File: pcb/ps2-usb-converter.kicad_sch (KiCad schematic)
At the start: 22 parts, among them J1 Mini-DIN-6

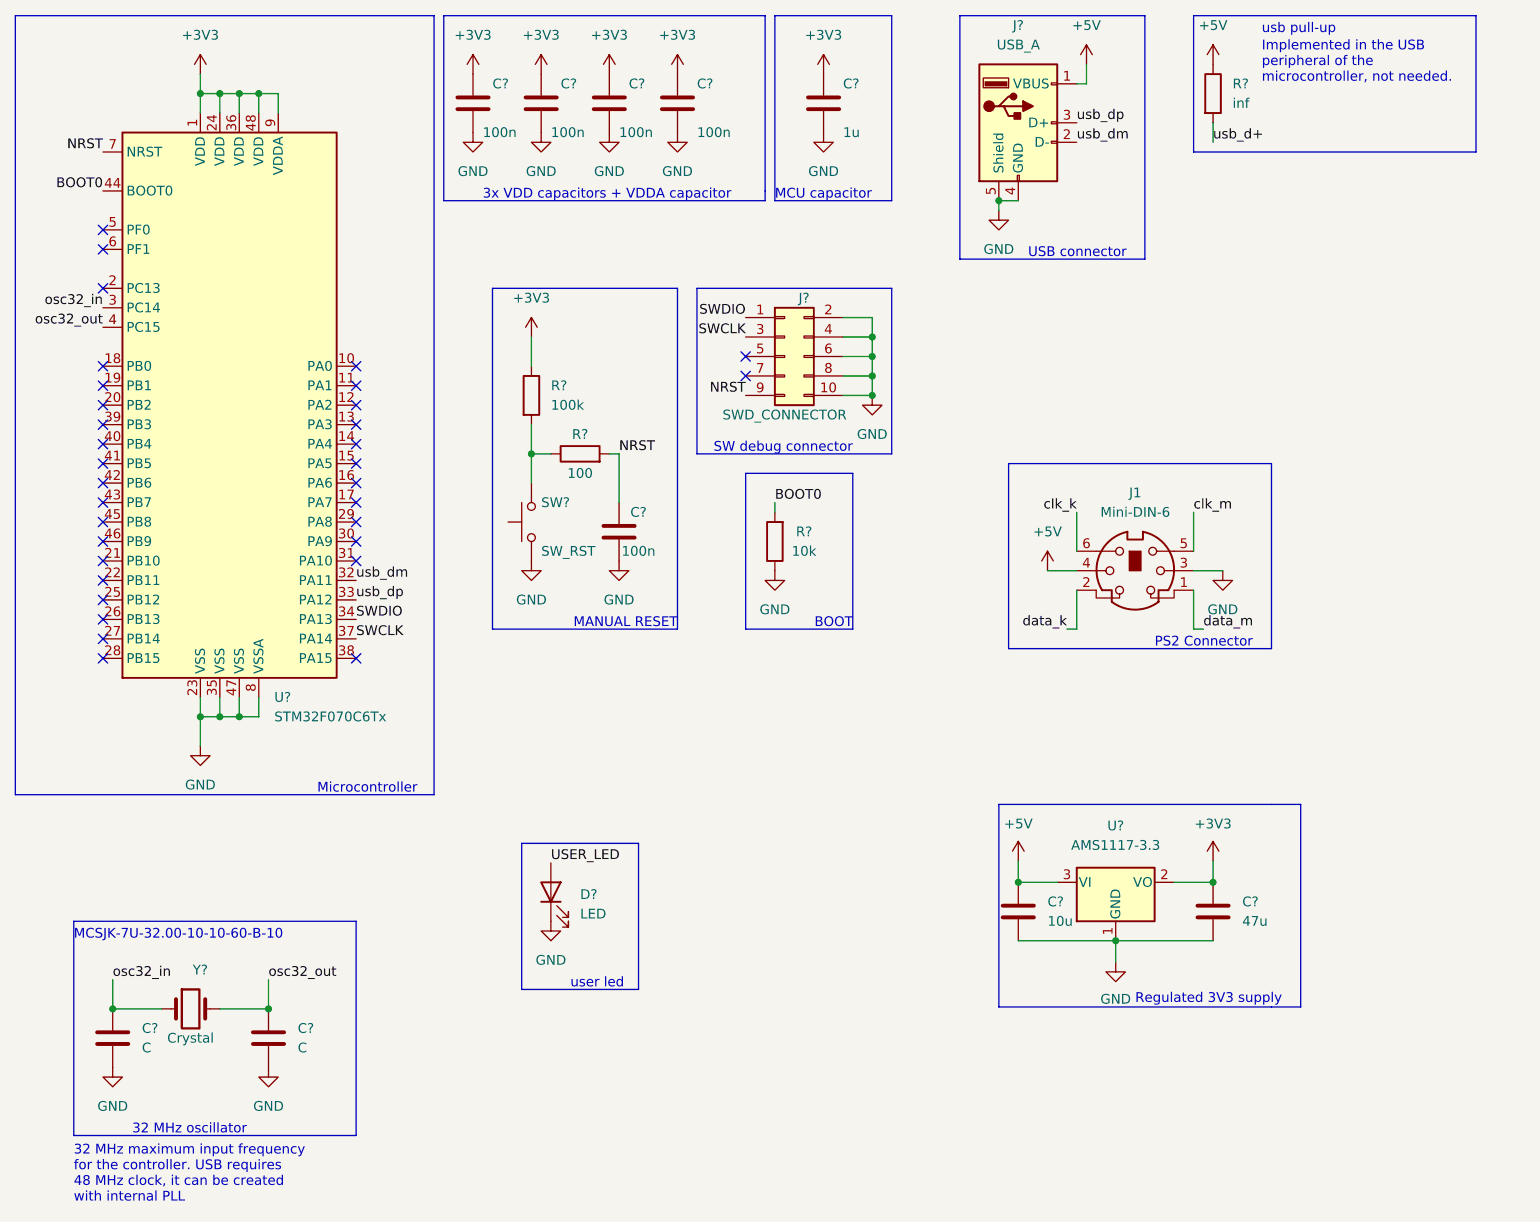
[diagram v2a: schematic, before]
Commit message: Add todo comments for schematic
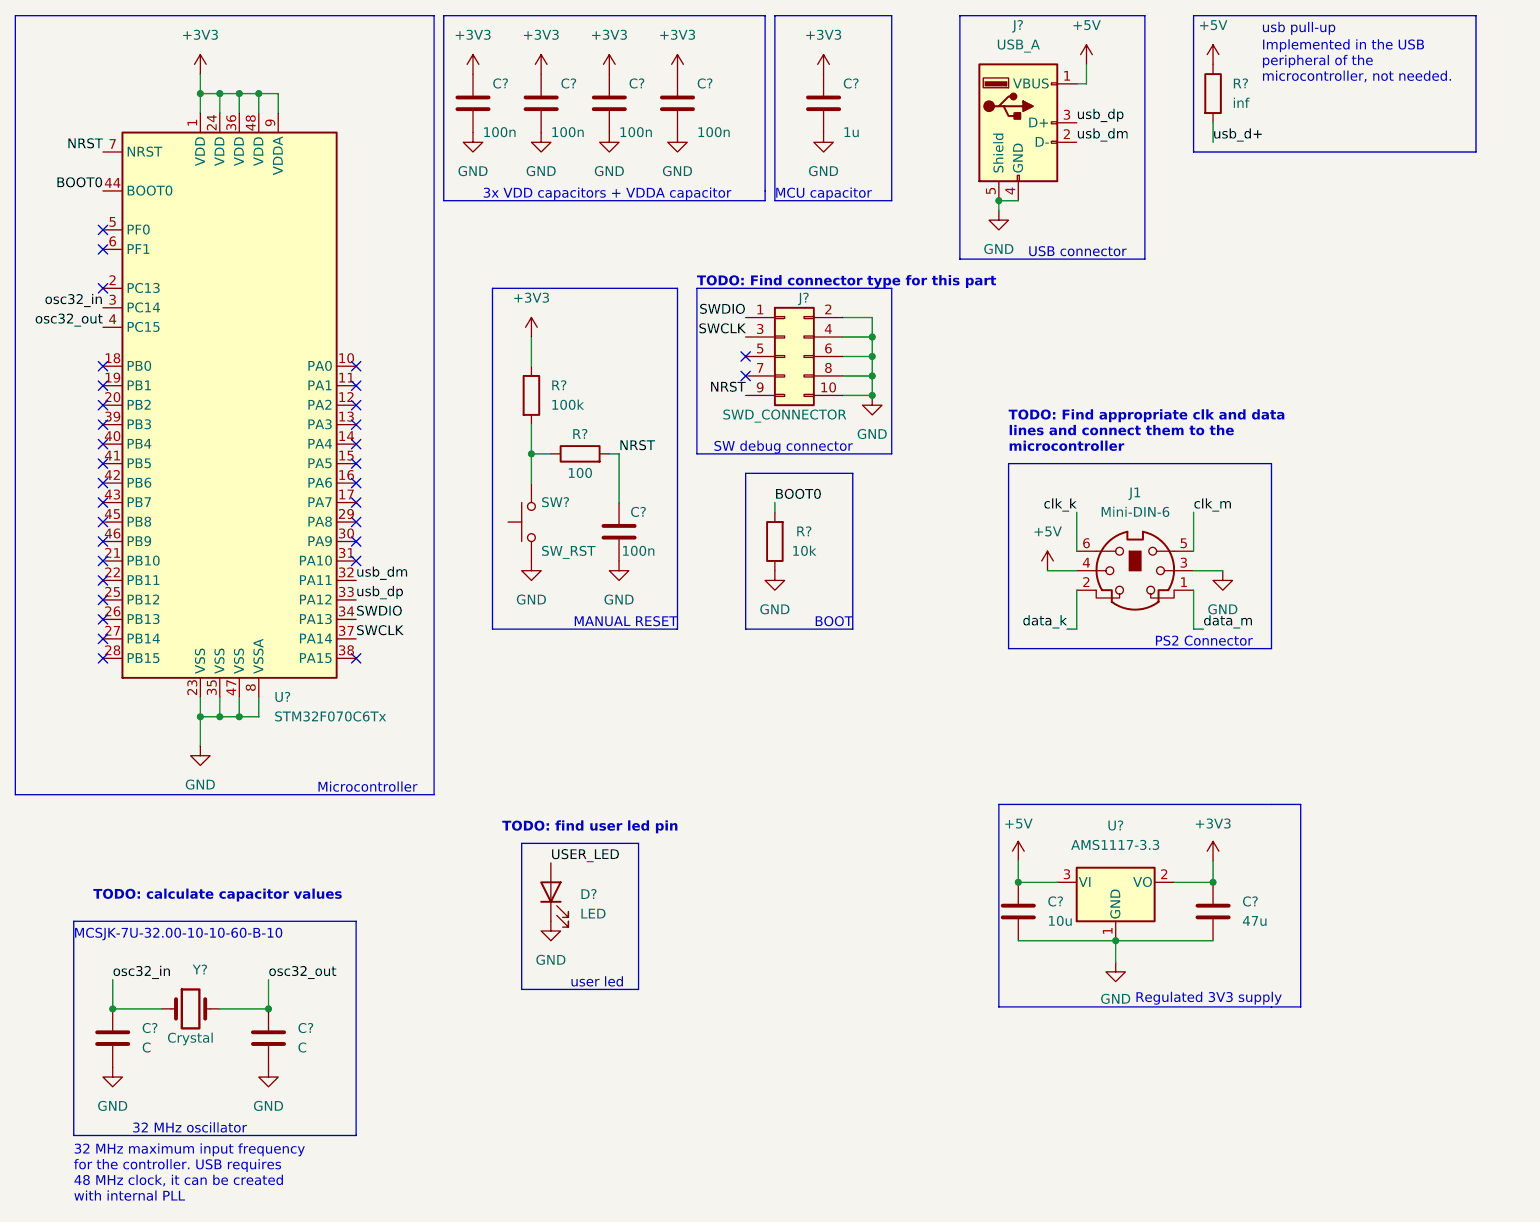
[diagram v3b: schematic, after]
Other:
- note added: "TODO: Find appropriate clk and data lines and connect them to the microcontroller"
- note added: "TODO: Find connector type for this part"
- note added: "TODO: calculate capacitor values"
- note added: "TODO: find user led pin"
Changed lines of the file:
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@@
     (effects (font (size 1.27 1.27)) (justify left bottom))
+  )
+  (text "TODO: find user led pin" (at 81.28 123.19 0)
+    (effects (font (size 1.27 1.27) (thickness 0.254) bold) (justify left bottom))
   )
   (text "USB connector" (at 149.86 48.26 0)
@@
     (effects (font (size 1.27 1.27)) (justify right bottom))
   )
+  (text "TODO: Find connector type for this part" (at 106.68 52.07 0)
+    (effects (font (size 1.27 1.27) bold) (justify left bottom))
+  )
   (text "MCU capacitor\n" (at 116.84 40.64 0)
     (effects (font (size 1.27 1.27)) (justify left bottom))
@@
     (effects (font (size 1.27 1.27)) (justify right bottom))
   )
+  (text "TODO: calculate capacitor values" (at 27.94 132.08 0)
+    (effects (font (size 1.27 1.27) (thickness 0.254) bold) (justify left bottom))
+  )
   (text "usb pull-up" (at 180.34 19.05 0)
     (effects (font (size 1.27 1.27)) (justify left bottom))
   )
+  (text "TODO: Find appropriate clk and data \nlines and connect them to the \nmicrocontroller"
+    (at 147.32 73.66 0)
+    (effects (font (size 1.27 1.27) (thickness 0.254) bold) (justify left bottom))
+  )
   (text "32 MHz maximum input frequency\nfor the controller. USB requires \n48 MHz clock, it can be created \nwith internal PLL"
